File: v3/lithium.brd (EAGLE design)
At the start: 71.8 x 54.6 mm, 53 parts, among them J1 batt, P8-1-2 bb-extra-gnd, P8-27-46 motors, P9-1-10 bb-pwr, P9-39-46 bb-extra-gnd, U1 TPS61088VQFN20, U1_C22 8.2nF, U1_CBST 100nF, U1_CCOMP 680PF, U1_CCOMP2 36pF, U1_CIN 0.47uF, U1_CIN2 100nF, U1_COUT 0.47uF, U1_CVCC 1uF, U1_L1 DR73-1R0-R, U1_RCOMP 38.3K Ohms, U1_RFBB 118K Ohms, U1_RFBT 470K Ohms, U1_RLIM 102K Ohms, U1_RT 261K Ohms, U4 TPS2113APWR, U4_C3 0.1uF, U4_C4 0.1uF, U4_RPG 100K Ohms, U5 MCP73833-FCI/UN, U5_C1 1.0uF, U5_C2 1.0uF, U5_R1 1K Ohm, U6 TPS61230A, U6_CBST 10 nF, U6_CFF 10pF, U6_CIN 22uF, U6_COUT 22uF, U6_RFBB 100K Ohms, U6_RFBT 316K Ohms

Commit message: Moving away from bb ideas.
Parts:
- removed P8-1-2: bb-extra-gnd, SparkFun-Connectors:1X02
- removed P9-39-46: bb-extra-gnd, SparkFun-Connectors:2X4
- added J2: 2X4-0.01"(2.54MM)-HEADERS, 32bits:2X4-0.01"(2.54MM)-HEADERS
- added U2: SI2312BDS-T1-GE3, 32bits:TO-236
- moved 3 8.00 mm to (66.9, 40.6)
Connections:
- removed net COPU: 5V.1, J1.1, MOTORS.1, P8-1-2.1, P8-1-2.2, P8-27-46.1, P8-27-46.15, P8-27-46.16, P8-27-46.19, P8-27-46.2, P8-27-46.20, P9-1-10.1, P9-1-10.2, P9-39-46.5, P9-39-46.6, P9-39-46.7, P9-39-46.8, R7.2, R9.1, U1.P$11, U1.P$12, U1.P$20, U1.P$21, U1.P$22, U1.P$23, U1.P$24, U1.P$25, U1_C22.1, U1_CCOMP.1, U1_CCOMP2.1, U1_CIN.1, U1_CIN2.1, U1_COUT.1, U1_CVCC.2, U1_RFBB.1, U1_RLIM.2, U4.2, U4.3, U4.5, U4_C3.2, U4_C4.2, U5.5, U5_C1.2, U5_C2.2, U5_R1.2, U6.P$6, U6_CIN.1, U6_COUT.1, U6_RFBB.2
- new net GND: 5V.1, J1.1, J2.5, J2.6, J2.7, MOTORS.1, P8-27-46.1, P8-27-46.15, P8-27-46.16, P8-27-46.19, P8-27-46.2, P8-27-46.20, P9-1-10.1, P9-1-10.2, R7.2, R9.1, U1.P$11, U1.P$12, U1.P$20, U1.P$21, U1.P$22, U1.P$23, U1.P$24, U1.P$25, U1_C22.1, U1_CCOMP.1, U1_CCOMP2.1, U1_CIN.1, U1_CIN2.1, U1_COUT.1, U1_CVCC.2, U1_RFBB.1, U1_RLIM.2, U4.2, U4.3, U4.5, U4_C3.2, U4_C4.2, U5.5, U5_C1.2, U5_C2.2, U5_R1.2, U6.P$6, U6_CIN.1, U6_COUT.1, U6_RFBB.2
- new net N$4: J2.8
- net U5_THERM: now also J2.1; no longer P9-39-46.1
- net VBAT: now also J2.3, J2.4; no longer P9-39-46.3, P9-39-46.4
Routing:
- net VBAT: track 40.6 -> 35.7 mm
- net U5_THERM: track 62.8 -> 59.2 mm
- net GND: track 0.00 -> 1.55 mm, vias 0 -> 111
- net COPU: track 1.55 -> 0.00 mm, vias 111 -> 0
- added copper zone on layer 1, net GND
- added copper zone on layer 16, net GND
- removed copper zone on layer 1, net COPU
- removed copper zone on layer 16, net COPU
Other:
- board size 71.8 x 54.6 mm -> 86.4 x 54.6 mm
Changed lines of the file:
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@@
 <setting verticaltext="up"/>
 </settings>
-<grid distance="0.05" unitdist="inch" unit="inch" style="dots" multiple="1" display="yes" altdistance="0.0025" altunitdist="inch" altunit="inch"/>
+<grid distance="8" unitdist="mm" unit="mm" style="dots" multiple="1" display="yes" altdistance="0.0025" altunitdist="inch" altunit="inch"/>
 <layers>
 <layer number="1" name="Top" color="4" fill="1" visible="yes" active="yes"/>
@@
 <board>
 <plain>
-<wire x1="14.605" y1="54.61" x2="73.66" y2="54.61" width="0.2032" layer="20"/>
+<wire x1="0" y1="41.91" x2="0" y2="12.7" width="0.2032" layer="20"/>
+<wire x1="0" y1="12.7" x2="12.7" y2="0" width="0.2032" layer="20" curve="90"/>
+<wire x1="12.7" y1="0" x2="73.66" y2="0" width="0.2032" layer="20"/>
+<wire x1="0" y1="41.91" x2="12.7" y2="54.61" width="0.2032" layer="20" curve="-90"/>
+<wire x1="12.7" y1="54.61" x2="73.66" y2="54.61" width="0.2032" layer="20"/>
 <wire x1="73.66" y1="54.61" x2="86.36" y2="41.91" width="0.2032" layer="20" curve="-90"/>
-<wire x1="14.605" y1="0" x2="73.66" y2="0" width="0.2032" layer="20"/>
 <wire x1="73.66" y1="0" x2="86.36" y2="12.7" width="0.2032" layer="20" curve="90"/>
 <wire x1="86.36" y1="12.7" x2="86.36" y2="41.91" width="0.2032" layer="20"/>
 <hole x="80.645" y="6.35" drill="3.175"/>
 <hole x="80.645" y="48.26" drill="3.175"/>
-<wire x1="15.875" y1="5.08" x2="14.605" y2="5.08" width="0.2032" layer="20"/>
-<wire x1="14.605" y1="5.08" x2="14.605" y2="0" width="0.2032" layer="20"/>
-<wire x1="14.605" y1="54.61" x2="14.605" y2="49.53" width="0.2032" layer="20"/>
-<wire x1="14.605" y1="49.53" x2="15.875" y2="49.53" width="0.2032" layer="20"/>
-<wire x1="15.875" y1="49.53" x2="22.225" y2="43.18" width="0.2032" layer="20" curve="-90"/>
-<wire x1="22.225" y1="43.18" x2="22.225" y2="11.43" width="0.2032" layer="20"/>
-<wire x1="22.225" y1="11.43" x2="15.875" y2="5.08" width="0.2032" layer="20" curve="-90"/>
-<hole x="70.46" y="43.305" drill="4.8"/>
-<hole x="70.46" y="11.305" drill="4.8"/>
+<hole x="78.46" y="43.305" drill="4.8"/>
+<hole x="78.46" y="11.305" drill="4.8"/>
 <hole x="30.46" y="43.305" drill="4.8"/>
 <hole x="30.46" y="11.305" drill="4.8"/>
+<hole x="14.46" y="43.305" drill="4.8"/>
+<hole x="14.46" y="11.305" drill="4.8"/>
+<hole x="5.715" y="48.26" drill="3.175"/>
+<hole x="5.715" y="6.35" drill="3.175"/>
 </plain>
 <attributes>
@@
 <attribute name="SUPPLIER" value="Dialight" x="160.02" y="-8.89" size="1.778" layer="27" rot="R90" display="off"/>
 </element>
-<element name="3" library="32bits" package="PERIODIC_SYMBOL_BACK" value="rev.0" x="74.93" y="40.64">
-<attribute name="ELEMENT" value="Li" x="39.37" y="-63.5" size="1.778" layer="27" display="off"/>
+<element name="3" library="32bits" package="PERIODIC_SYMBOL_BACK" value="rev.0" x="66.93" y="40.64">
+<attribute name="ELEMENT" value="Li" x="31.37" y="-63.5" size="1.778" layer="27" display="off"/>
 </element>
 <element name="5V" library="Dialight_By_element14_Batch_1" package="LED_597-3311-407F" value="QTLP650C-4" x="43.18" y="5.08" smashed="yes" rot="R90">
@@
 <attribute name="SF_ID" value="PRT-0778" x="19.685" y="50.165" size="1.778" layer="27" display="off"/>
 </element>
-<element name="P9-39-46" library="SparkFun-Connectors" package="2X4" value="bb-extra-gnd" x="71.755" y="51.435" smashed="yes"/>
-<element name="P8-1-2" library="SparkFun-Connectors" package="1X02" value="bb-extra-gnd" x="19.685" y="1.905" smashed="yes" rot="R90"/>
 <element name="U6" library="32bits" package="VQFN7" value="TPS61230A" x="55.88" y="36.83" smashed="yes" rot="R270">
 <attribute name="NAME" x="54.61" y="39.37" size="1.016" layer="21" font="vector" ratio="1" align="bottom-center"/>
@@
 </element>
 <element name="R9" library="32bits" package="1206" value="10k" x="30.48" y="27.94"/>
+<element name="U2" library="32bits" package="TO-236" value="SI2312BDS-T1-GE3" x="15.24" y="-11.43">
+<attribute name="MANUFACTURER_PART_NUMBER" value="SI2312BDST1GE3" x="15.24" y="-11.43" size="0.6096" layer="27" ratio="1" display="off"/>
+<attribute name="VENDOR" value="Vishay" x="15.24" y="-11.43" size="0.6096" layer="27" ratio="1" display="off"/>
+</element>
+<element name="J2" library="32bits" package="2X4-0.01&quot;(2.54MM)-HEADERS" value="2X4-0.01&quot;(2.54MM)-HEADERS" x="67.945" y="48.895"/>
 </elements>
 <signals>
-<signal name="COPU">
+<signal name="GND">
 <contactref element="U1" pad="P$21"/>
 <contactref element="U1_CIN" pad="1"/>
@@
 <contactref element="P9-1-10" pad="1"/>
 <contactref element="P9-1-10" pad="2"/>
-<contactref element="P8-1-2" pad="2"/>
-<contactref element="P8-1-2" pad="1"/>
-<contactref element="P9-39-46" pad="6"/>
-<contactref element="P9-39-46" pad="8"/>
-<contactref element="P9-39-46" pad="5"/>
-<contactref element="P9-39-46" pad="7"/>
 <contactref element="P8-27-46" pad="1"/>
 <contactref element="P8-27-46" pad="2"/>
@@
 <contactref element="R9" pad="1"/>
 <polygon width="0.2032" layer="1" thermals="no" rank="4">
-<vertex x="13.97" y="-1.27"/>
+<vertex x="-1.27" y="-1.27"/>
 <vertex x="88.9" y="-1.27"/>
 <vertex x="88.9" y="55.88"/>
-<vertex x="13.97" y="55.88"/>
+<vertex x="-1.27" y="55.88"/>
 </polygon>
 <polygon width="0.2032" layer="16" thermals="no" rank="4">
-<vertex x="13.97" y="55.88"/>
+<vertex x="-1.27" y="55.88"/>
 <vertex x="87.63" y="55.88"/>
 <vertex x="87.63" y="-1.27"/>
-<vertex x="13.97" y="-1.27"/>
+<vertex x="-1.27" y="-1.27"/>
 </polygon>
 <via x="31.75" y="36.83" extent="1-16" drill="0.3302"/>
@@
 <via x="69.1515" y="17.526" extent="1-16" drill="0.3302"/>
 <via x="66.8655" y="28.7655" extent="1-16" drill="0.3302"/>
+<contactref element="J2" pad="5"/>
+<contactref element="J2" pad="7"/>
+<contactref element="J2" pad="6"/>
 </signal>
 <signal name="SW">
@@
 <contactref element="U4" pad="8"/>
 <contactref element="U4_C4" pad="1"/>
-<contactref element="P9-39-46" pad="3"/>
-<contactref element="P9-39-46" pad="4"/>
-<wire x1="70.485" y1="52.705" x2="70.485" y2="50.165" width="0.762" layer="1"/>
-<wire x1="70.485" y1="50.165" x2="70.485" y2="47.75174375" width="0.762" layer="1"/>
 <wire x1="69.7791375" y1="47.062578125" x2="70.485" y2="47.75174375" width="0.762" layer="1"/>
 <wire x1="69.7791375" y1="47.062578125" x2="67.272" y2="44.61474375" width="0.762" layer="1"/>
@@
 <wire x1="68.8213" y1="47.8155" x2="69.026215625" y2="47.8155" width="0.762" layer="1"/>
 <wire x1="69.026215625" y1="47.8155" x2="69.7791375" y2="47.062578125" width="0.762" layer="1"/>
+<contactref element="J2" pad="3"/>
+<contactref element="J2" pad="4"/>
+<wire x1="70.485" y1="47.75174375" x2="70.485" y2="51.625" width="0" layer="19" extent="1-1"/>
+<wire x1="70.485" y1="46.165" x2="69.7791375" y2="47.062578125" width="0" layer="19" extent="1-1"/>
 </signal>
 <signal name="VUSB">
@@
 <signal name="U5_THERM">
 <contactref element="U5" pad="8"/>
-<contactref element="P9-39-46" pad="1"/>
 <wire x1="69.3547" y1="26.67" x2="68.3895" y2="26.67" width="0.254" layer="1"/>
 <wire x1="68.3895" y1="26.67" x2="67.691" y2="27.432" width="0.381" layer="1"/>
@@
 <wire x1="66.3575" y1="45.0215" x2="67.8942" y2="46.5582" width="0.381" layer="1"/>
 <wire x1="67.8942" y1="46.5582" x2="67.8942" y2="46.5963" width="0.381" layer="1"/>
-<wire x1="67.8942" y1="46.5963" x2="67.945" y2="50.165" width="0.381" layer="1"/>
 <contactref element="R9" pad="2"/>
 <via x="66.04" y="29.21" extent="1-16" drill="0.381"/>
@@
 <via x="49.53" y="27.94" extent="1-16" drill="0.381"/>
 <wire x1="31.88" y1="27.94" x2="49.53" y2="27.94" width="0.381" layer="1"/>
+<contactref element="J2" pad="1"/>
+<wire x1="67.8942" y1="46.5582" x2="67.945" y2="46.165" width="0" layer="19" extent="1-1"/>
 </signal>
 <signal name="U4_ILIM">
@@
 <wire x1="60.866" y1="49.276" x2="60.85" y2="49.26" width="0.762" layer="1"/>
 </signal>
+<signal name="N$4">
+<contactref element="J2" pad="8"/>
+</signal>
 </signals>

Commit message: New lithium mechanically complete.
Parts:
- removed P8-27-46: motors, SparkFun-Connectors:2X10
- removed P9-1-10: bb-pwr, SparkFun-Connectors:2X5
- removed U2: SI2312BDS-T1-GE3, 32bits:TO-236
- added J3: motor, 32bits:2X4-0.01"(2.54MM)-SOCKET
- added Q1: (no value), 32bits:SO-8
- added R10: 0Ohm, Vishay_By_element14_Batch_1:RESC2013X65N
- J2: value 2X4-0.01"(2.54MM)-HEADERS -> battery; device 32bits:2X4-0.01"(2.54MM)-HEADERS -> 32bits:2X4-0.01"(2.54MM)-SOCKET
- S1: value PWR -> SS312SAH4; device 32bits:AS11CH-TOP -> 32bits:SS312SAH4
- moved 3 56.8 mm to (11.1, 30.5), flipped to the bottom
- moved R7 20.0 mm to (82.9, 30.5)
- moved U5_C1 19.9 mm to (82.4, 33.0), turned to 270 degrees
- moved U4_RPG 18.5 mm to (83.0, 26.9), turned to 90 degrees
- moved U4_C4 15.3 mm to (69.2, 40.3)
- moved U5_R1 15.0 mm to (75.4, 38.1), turned to 90 degrees
- moved U5 13.8 mm to (77.9, 35.6), turned to 180 degrees
- moved R8 13.5 mm to (54.5, 49.3)
- moved U5_C2 11.8 mm to (69.2, 38.6)
- moved J1 11.5 mm to (45.7, 49.0)
- moved U4 11.4 mm to (78.1, 28.9), turned to 180 degrees
- moved U1_COUT 8.38 mm to (60.6, 12.8)
- moved L2 8.03 mm to (65.2, 35.2)
- moved U1 8.03 mm to (62.9, 17.1)
- moved U1_CBST 8.03 mm to (61.5, 20.6)
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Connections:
- removed net N$4: J2.8
- new net THERM_EXT: J2.P$3, R10.1
- new net VBAT_RAW: J2.P$1, Q1.P$5, Q1.P$6, Q1.P$7, Q1.P$8, Q1.P$9, R8.1
- net GND: now also J2.P$5, J2.P$6, J3.P$1, J3.P$2, J3.P$3, J3.P$4, J3.P$7, J3.P$8, Q1.P$4; no longer J2.5, J2.6, J2.7, P8-27-46.1, P8-27-46.15, P8-27-46.16, P8-27-46.19, P8-27-46.2, P8-27-46.20, P9-1-10.1, P9-1-10.2
- net MOT_6V: now also J3.P$5, J3.P$6; no longer P8-27-46.17, P8-27-46.18
- net S1_U4OUT: now also S1.P$1; no longer S1.P$2
- net SYS_5V: now also J2.P$4; no longer P9-1-10.7, P9-1-10.8
- net U5_THERM: now also R10.2; no longer J2.1
- net VBAT: now also Q1.P$1, Q1.P$2, Q1.P$3; no longer J2.3, J2.4, R8.1
- net VCC: now also S1.P$2; no longer S1.P$1
- net VUSB: now also J2.P$7; no longer P8-27-46.13, P8-27-46.14
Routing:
- net STAT1: track 59.9 -> 0.00 mm, vias 2 -> 1
- net U5_THERM: track 59.2 -> 25.3 mm, vias 2 -> 1
- net VBAT_RAW: track 0.00 -> 25.6 mm
- net VCC: track 51.4 -> 33.4 mm
- net U5_NPG: track 47.5 -> 61.6 mm
- net VUSB: track 95.8 -> 105.8 mm, vias 2 -> 1
- net MOT_6V: track 7.76 -> 15.6 mm
- net VBAT: track 35.7 -> 39.4 mm
- net S1_U4OUT: track 0.01 -> 3.47 mm
- net LOCAL_VBAT: track 6.70 -> 4.20 mm
- net U4_ILIM: track 2.00 -> 0.00 mm
- net GND: track 1.55 -> 0.00 mm, vias 111 -> 45
- net U4_STAT: track 52.1 -> 51.0 mm
- added copper zone on layer 1, net VBAT_RAW
- removed copper zone on layer 1, net GND
- removed copper zone on layer 16, net GND
- removed copper zone on layer 1, net S1_U4OUT
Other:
- outline, holes or cut-outs redrawn

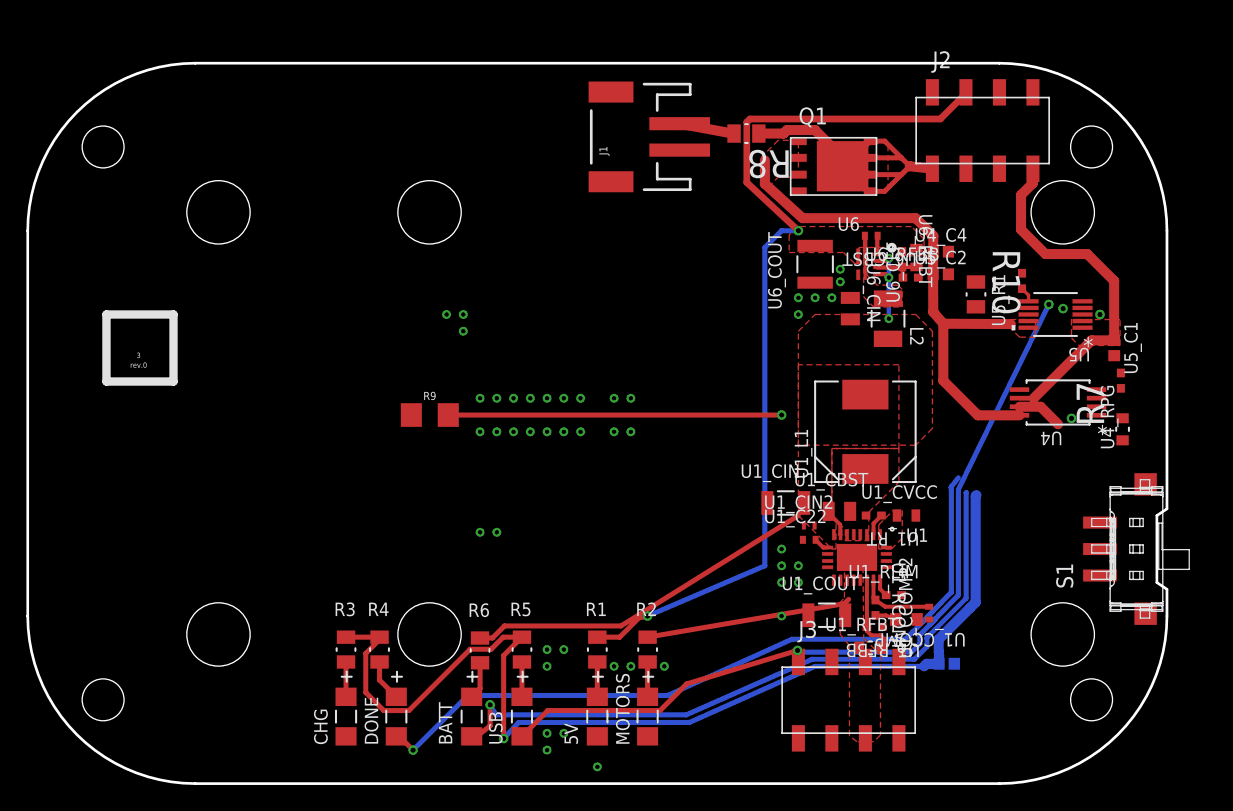
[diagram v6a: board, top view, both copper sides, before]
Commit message: Lithium with ATTiny84 for ADC.
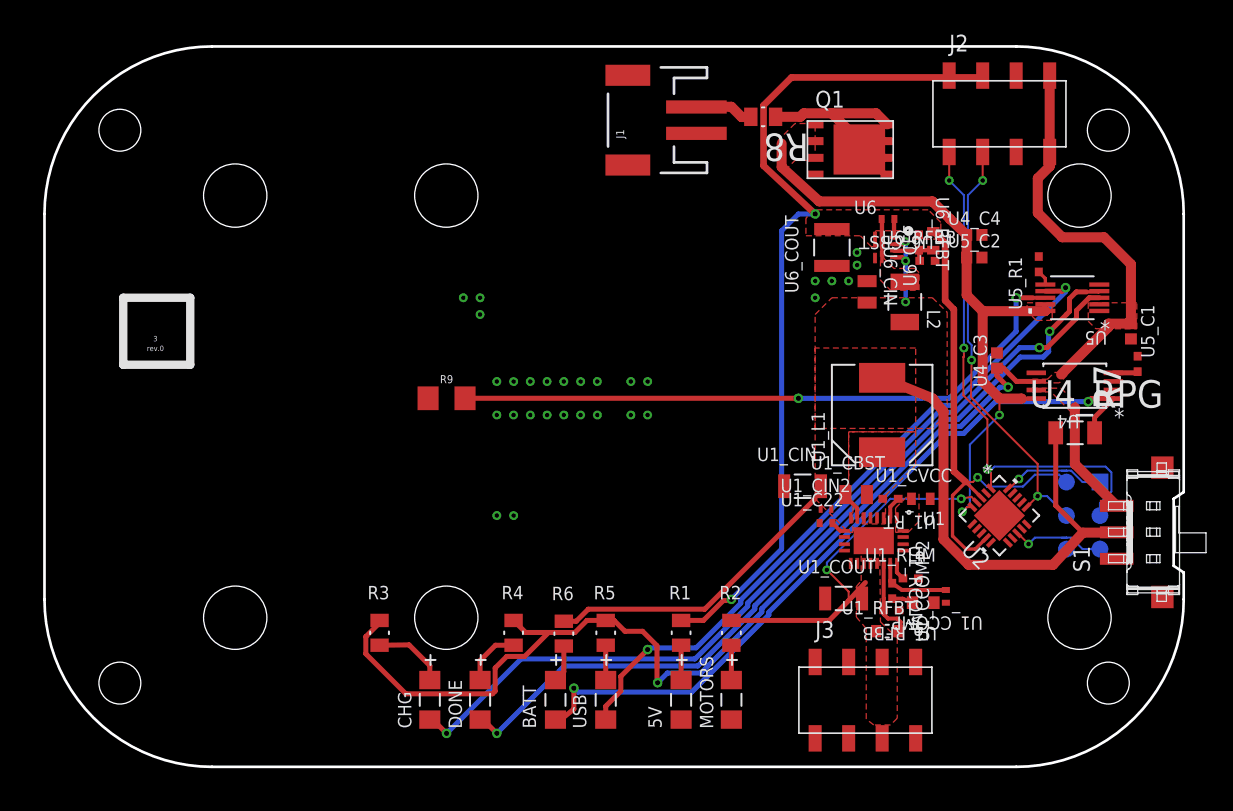
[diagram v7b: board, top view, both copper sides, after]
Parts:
- removed R10: 0Ohm, Vishay_By_element14_Batch_1:RESC2013X65N
- added J4: AVR_ISP, 32bits:.1-ISP-PADS
- added U2: ATTINY84-20MU, 32bits:20M1
- U4_RPG: device Vishay_By_element14_Batch_1:RESC1608X60N -> Vishay_By_element14_Batch_1:RESC3216X71N
- moved U4_C3 23.3 mm to (73.5, 32.1), flipped to the top, turned to 90 degrees
- moved R4 10.2 mm to (36.8, 11.4)
- moved 5V 6.48 mm to (49.5, 6.35)
- moved BATT 6.48 mm to (40.0, 6.35)
- moved CHG 6.48 mm to (30.5, 6.35)
- moved MOTORS 6.48 mm to (53.3, 6.35)
- moved R1 6.48 mm to (49.5, 11.4)
- moved R2 6.48 mm to (53.3, 11.4)
- moved R6 6.48 mm to (40.6, 11.4)
- moved DONE 6.48 mm to (34.3, 6.35)
- moved R5 6.48 mm to (43.8, 11.4)
- moved USB 6.48 mm to (43.8, 6.35)
- moved U4_RPG 3.60 mm to (79.4, 26.6), turned to 0 degrees
- moved R3 2.84 mm to (26.7, 11.4)
- moved U4_C4 2.84 mm to (71.8, 41.6)
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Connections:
- removed net THERM_EXT: J2.P$3, R10.1
- removed net VBAT_RAW: J2.P$1, Q1.P$5, Q1.P$6, Q1.P$7, Q1.P$8, Q1.P$9, R8.1
- new net !RESET: J4.5, U2.13
- new net MISO: J4.1, U2.20
- new net MOSI/SDA: J2.P$3, J4.4, U2.16
- new net SCK: J2.P$1, J4.3, U2.1
- new net VBAT_MON: Q1.P$5, Q1.P$6, Q1.P$7, Q1.P$8, Q1.P$9, R8.1
- net GND: now also J4.6, U2.8
- net MOT_6V: now also U2.4
- net SYS_5V: now also J2.P$2, J4.2, U2.3, U2.9
- net U5_THERM: no longer R10.2
- net VBAT: now also U2.5
- net VUSB: now also J2.P$8
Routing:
- net STAT1: track 0.00 -> 65.3 mm, vias 1 -> 2
- net SCK: track 0.00 -> 40.1 mm, vias 0 -> 3
- net VCC: track 33.4 -> 68.0 mm
- net SYS_5V: track 68.9 -> 102.8 mm, vias 2 -> 3
- net MOSI/SDA: track 0.00 -> 32.7 mm, vias 0 -> 3
- net VBAT_RAW: track 25.6 -> 0.00 mm
- net U5_THERM: track 25.3 -> 48.6 mm, vias 1 -> 2
- net VBAT_MON: track 0.00 -> 23.1 mm
- net MOT_6V: track 15.6 -> 28.5 mm, vias 0 -> 2
- net VBAT: track 39.4 -> 49.6 mm, vias 0 -> 2
- net U5_NPG: track 61.6 -> 51.6 mm
- net MISO: track 0.00 -> 8.25 mm, vias 0 -> 1
- net !RESET: track 0.00 -> 7.52 mm, vias 0 -> 1
- net STAT2: track 55.5 -> 62.9 mm
- net U4_STAT: track 51.0 -> 56.8 mm
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- added copper zone on layer 1, net S1_U4OUT
- removed copper zone on layer 1, net VBAT_RAW

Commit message: Lithium schematic complete.
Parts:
- added D1: 1SS367,H3F, SparkFun-DiscreteSemi:SOD-323
- added Q1_R1: 100k, SparkFun-Resistors:0603
- added U2_C1, U2_C2: 22uF, 32bits:0402
- added U2_R1, U2_R2: 10k, SparkFun-Resistors:0402
- moved Q1 2.06 mm to (60.9, 51.7)
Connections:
- new net Q1_GATE: D1.A, Q1.P$4, Q1_R1.2
- net GND: now also Q1_R1.1, U2_C1.2, U2_C2.1; no longer Q1.P$4
- net MOSI/SDA: now also U2_R1.1
- net SCK: now also U2_R2.1
- net SYS_5V: now also U2_C1.1, U2_C2.2, U2_R1.2, U2_R2.2
- net VBAT: now also D1.C
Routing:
- net SYS_5V: track 102.8 -> 122.2 mm
- net VBAT: track 49.6 -> 55.2 mm
- net SCK: track 40.1 -> 44.9 mm
- net Q1_GATE: track 0.00 -> 4.71 mm
- net VBAT_MON: track 23.1 -> 20.7 mm
- net MISO: track 8.25 -> 9.66 mm
- net MOSI/SDA: track 32.7 -> 34.1 mm
- net VCC: track 68.0 -> 69.0 mm
- net !RESET: track 7.52 -> 8.30 mm
- added copper zone on layer 1, net GND
- added copper zone on layer 16, net GND
